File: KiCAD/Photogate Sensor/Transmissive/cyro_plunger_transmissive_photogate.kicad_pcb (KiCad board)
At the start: 2 copper layers, 122 x 70 mm, 46 parts, among them J2 FFC Socket, J3 USB_B_Micro, J4 UPDI socket, J6 Conn_01x03_Socket, Q1 Q_NMOS_GSD, Q2 Q_NMOS_GSD, Q3 Q_NMOS_GSD, Q4 Q_NMOS_GSD, U1 5V LDO, U2 Opamp_Dual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

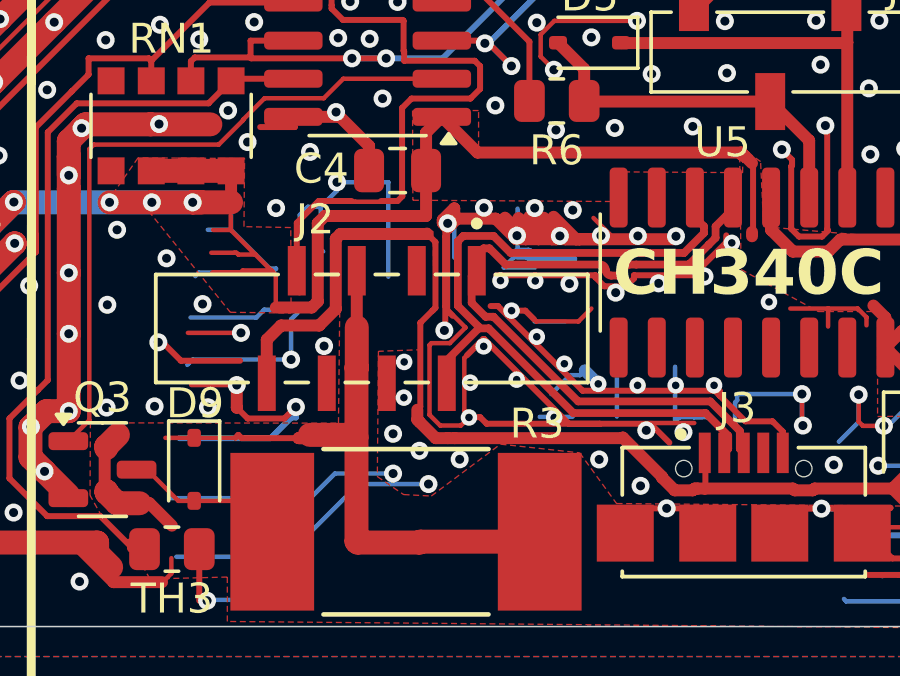
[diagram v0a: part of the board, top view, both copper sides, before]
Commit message: Place Gnds closer to data lines on FFC
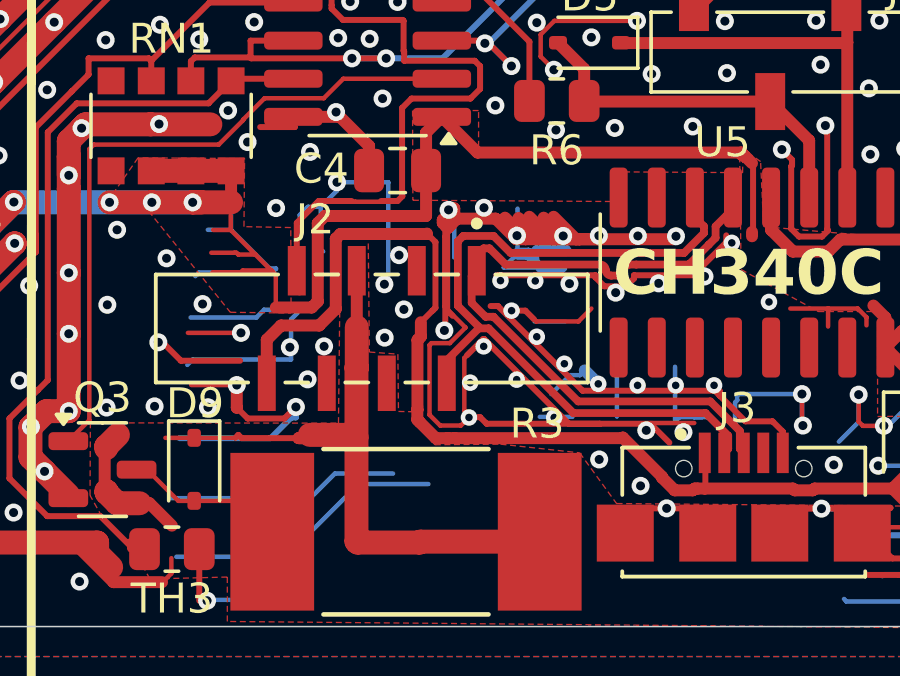
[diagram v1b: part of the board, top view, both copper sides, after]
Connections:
- J2 pad 3: +12V -> GND
- J2 pad 4: GND -> +12V
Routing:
- net GND: track 828.0 -> 827.6 mm, vias 588 -> 584

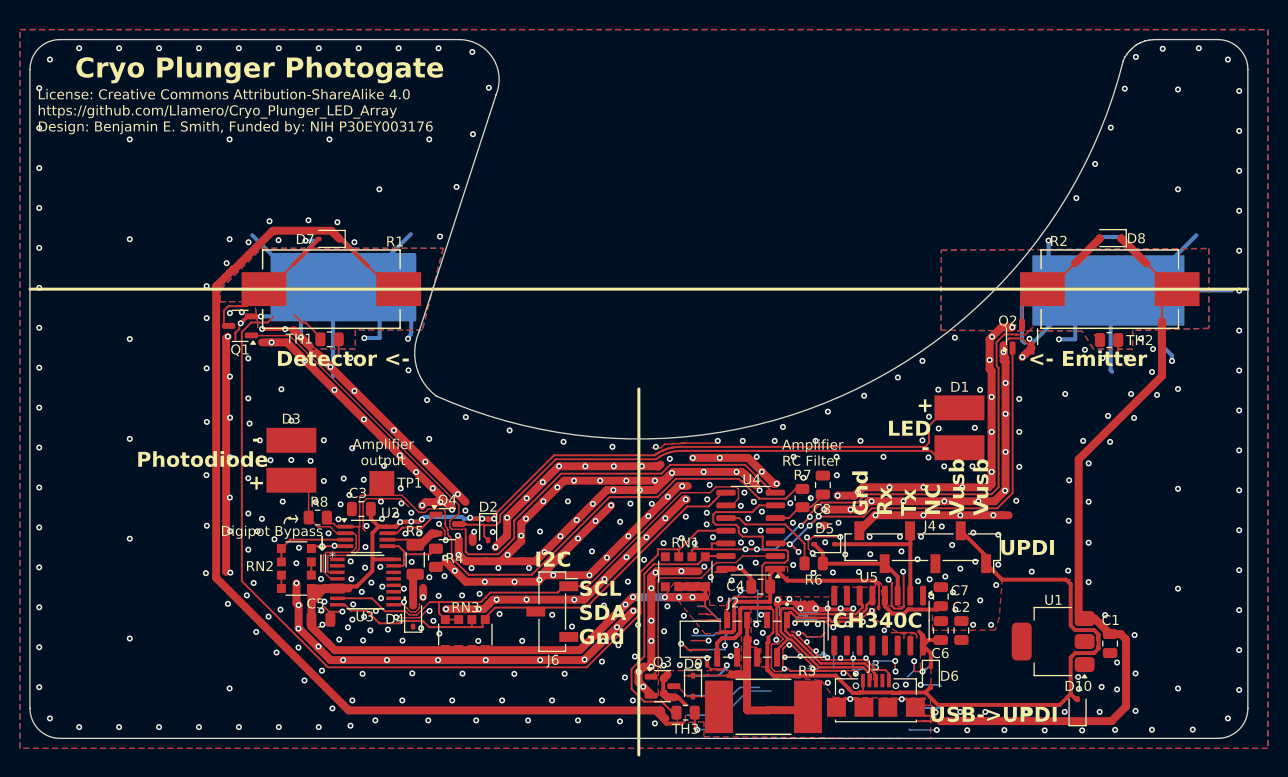
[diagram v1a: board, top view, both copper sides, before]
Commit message: More ground optimizations
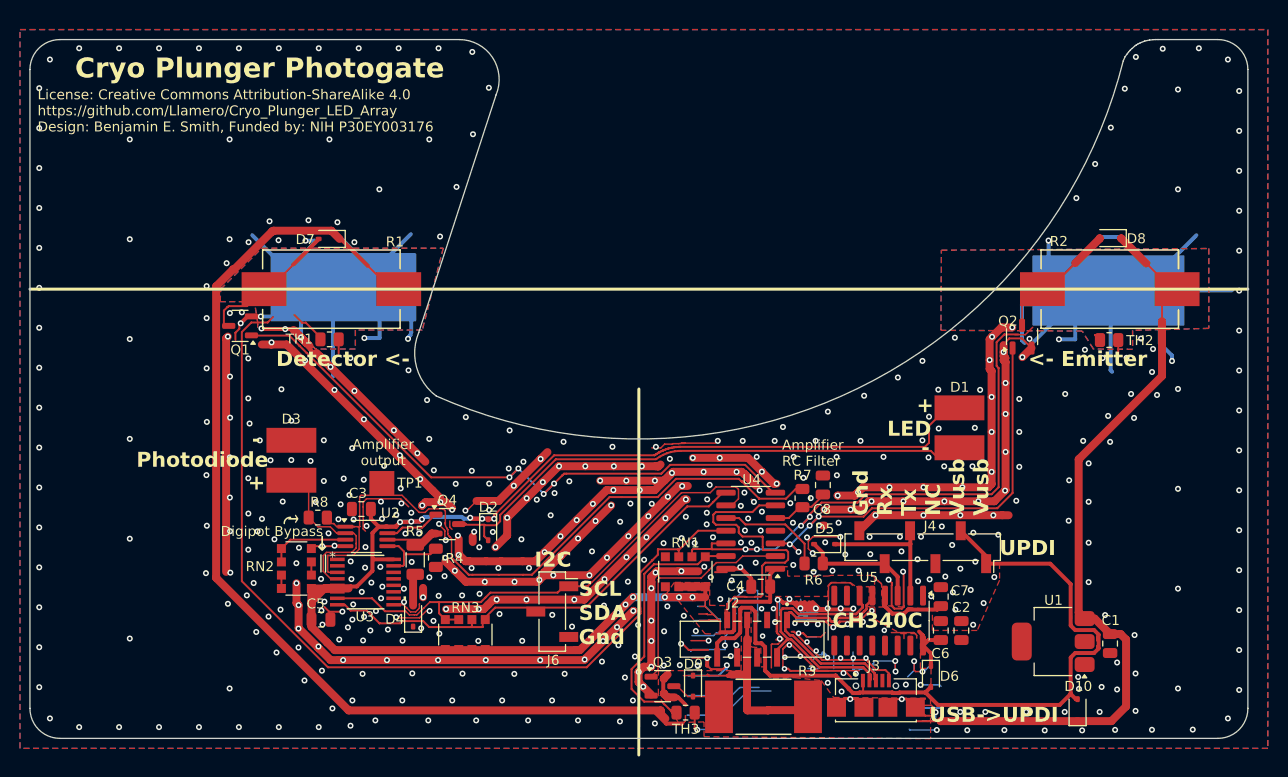
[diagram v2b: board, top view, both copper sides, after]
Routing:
- net +5V: track 185.0 -> 171.5 mm
- net GND: track 827.6 -> 816.1 mm, vias 584 -> 586
- net /Heater1: track 72.1 -> 65.8 mm, vias 0 -> 4
- net /Vusb: track 81.3 -> 80.0 mm

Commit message: Panelize boards - improve 12V thermal pad
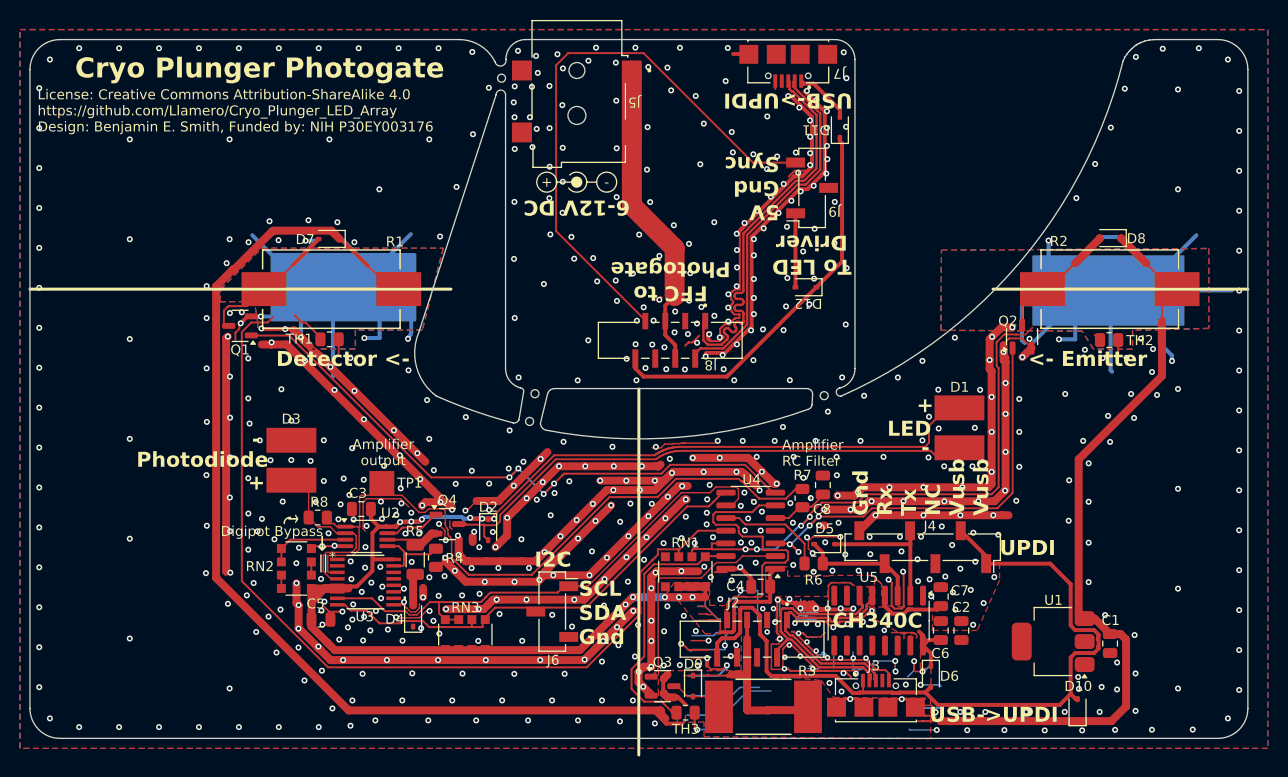
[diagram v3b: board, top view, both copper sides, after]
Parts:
- added D11: D_Schottky, Diode_SMD:D_SOD-323, F.Cu at (181.1, 108.8)
- added D12: D_Schottky, Diode_SMD:D_SOD-323, F.Cu at (177.7, 124.8)
- added H2: ~, Custom:mouse bite, F.Cu at (147.2, 103.9)
- added H3: ~, Custom:mouse bite, F.Cu at (150.6, 135.5)
- added H4: ~, Custom:mouse bite, F.Cu at (179.6, 135.7)
- added H5: ~, Custom:mouse bite, F.Cu at (150.1, 138.2)
- added J5: DC Jack, Custom:TENSILITY_54-00165, F.Cu at (154.8, 105.3)
- added J7: USB_B_Micro, Custom:CUI_UJ2-MIBH-G-SMT-TR, F.Cu at (176.0, 101.5)
- added J8: FFC Socket, Custom:AMPHENOL_SFW8S-2STE1LF, F.Cu at (164.1, 130.1)
- added J9: Conn_01x03_Socket, Connector_PinSocket_2.54mm:PinSocket_1x03_P2.54mm_Vertical_SMD_Pin1Right, F.Cu at (178.3, 114.9)
- added SYM1: Logo_Open_Hardware_Small, Custom:polarity, F.Cu at (154.6, 115.6)
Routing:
- net GND: track 816.1 -> 893.4 mm, vias 586 -> 736
- net /Comp Out: track 30.1 -> 88.5 mm
- net /D+: track 23.9 -> 64.6 mm
- net /Vusb: track 80.0 -> 118.9 mm
- net /D-: track 26.0 -> 62.1 mm
- net +12V: track 214.2 -> 245.7 mm
- net Net-(D12-A): track 0.00 -> 7.47 mm
- net Net-(D11-A): track 0.00 -> 5.77 mm
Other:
- outline, holes or cut-outs redrawn
- board text added: "5V Gnd Sync"
- board text added: "6-12V DC"
- board text added: "FFC to Photogate"
- board text added: "To LED Driver"

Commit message: replace silicon updi diode with schottky
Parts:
- D5: value D -> D_Schottky
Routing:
- net GND: vias 736 -> 739
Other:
- board text added: "Amplifier Output"
- board text removed: "Amplifier output"
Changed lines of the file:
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@@
 			)
 		)
-		(property "Value" "D"
+		(property "Value" "D_Schottky"
 			(at 0.1 1.9 0)
 			(layer "F.Fab")
@@
 			)
 		)
-		(property "Datasheet" "https://www.mccsemi.com/pdf/Products/1N4148WX(SOD-323).pdf"
+		(property "Datasheet" "https://toshiba.semicon-storage.com/info/docget.jsp?did=14077&prodName=CUS10S30"
 			(at 0 0 180)
 			(unlocked yes)
@@
 			)
 		)
-		(property "Description" "Diode 75 V 150mA Surface Mount SOD-323"
+		(property "Description" "Diode 30 V 1A Surface Mount USC"
 			(at 0 0 180)
 			(unlocked yes)
@@
 			)
 		)
-		(property "Manufacturer" "MCC (Micro Commercial Components)"
+		(property "Manufacturer" "Toshiba Semiconductor and Storage"
 			(at 0 0 180)
 			(unlocked yes)
@@
 			)
 		)
-		(property "Part" "1N4148WX-TP"
+		(property "Part" "CUS10S30,H3F"
 			(at 0 0 180)
 			(unlocked yes)
@@
 		)
 		(property "Value" "DC Jack"
-			(at 6.985 -8.8625 360)
+			(at 6.985 -8.8625 0)
 			(layer "F.Fab")
 			(effects
@@
 		)
 		(property "Footprint" "Custom:TENSILITY_54-00165"
-			(at 0 0 360)
+			(at 0 0 0)
 			(layer "F.Fab")
 			(hide yes)
@@
 		)
 		(property "Datasheet" "https://tensility.s3.us-west-2.amazonaws.com/uploads/pdffiles/54-00165.pdf"
-			(at 0 0 360)
+			(at 0 0 0)
 			(layer "F.Fab")
 			(hide yes)
@@
 		)
 		(property "Description" "Power Barrel Connector Jack 2.50mm ID (0.098\"), 5.50mm OD (0.217\") Surface Mount, Right Angle"
-			(at 0 0 360)
+			(at 0 0 0)
 			(layer "F.Fab")
 			(hide yes)
@@
 		)
 		(property "Value" "Conn_01x03_Socket"
-			(at 0 5.41 360)
+			(at 0 5.41 0)
 			(layer "F.Fab")
 			(effects
@@
 		)
 		(property "Value" "USB_B_Micro"
-			(at 9.335 -4.335 360)
+			(at 9.335 -4.335 0)
 			(layer "F.Fab")
 			(effects
@@
 		)
 		(property "Footprint" "Custom:CUI_UJ2-MIBH-G-SMT-TR"
-			(at 0 0 360)
+			(at 0 0 0)
 			(layer "F.Fab")
 			(hide yes)
@@
 		)
 		(property "Datasheet" "https://www.cuidevices.com/product/resource/uj2-mibh-g-smt-tr.pdf"
-			(at 0 0 360)
+			(at 0 0 0)
 			(layer "F.Fab")
 			(hide yes)
@@
 		)
 		(property "Description" "USB JACK, 2.0, MICRO B TYPE, 5 P"
-			(at 0 0 360)
+			(at 0 0 0)
 			(layer "F.Fab")
 			(hide yes)
@@
 		)
 		(fp_text user "PCB EDGE"
-			(at 5.325 1.325 360)
+			(at 5.325 1.325 0)
 			(layer "F.Fab")
 			(effects
@@
 		)
 		(property "Value" "D_Schottky"
-			(at 0.1 1.9 360)
+			(at 0.1 1.9 0)
 			(layer "F.Fab")
 			(effects
@@
 		)
 		(fp_text user "${REFERENCE}"
-			(at 0 -1.85 360)
+			(at 0 -1.85 0)
 			(layer "F.Fab")
 			(effects
@@
 		)
 		(fp_text user "-"
-			(at -3.2 1.35 360)
+			(at -3.2 1.35 0)
 			(layer "F.SilkS")
 			(effects
@@
 		)
 		(fp_text user "+"
-			(at 2.8 1.35 360)
+			(at 2.8 1.35 0)
 			(layer "F.SilkS")
 			(effects
@@
 		)
 		(property "Value" "FFC Socket"
-			(at 6.825 4.445 360)
+			(at 6.825 4.445 0)
 			(layer "F.Fab")
 			(effects
@@
 		)
 		(property "Footprint" "Custom:AMPHENOL_SFW8S-2STE1LF"
-			(at 0 0 360)
+			(at 0 0 0)
 			(layer "F.Fab")
 			(hide yes)
@@
 		)
 		(property "Datasheet" "https://cdn.amphenol-cs.com/media/wysiwyg/files/documentation/datasheet/flex/flexconnectors_100mm_sfw_s.pdf"
-			(at 0 0 360)
+			(at 0 0 0)
 			(layer "F.Fab")
 			(hide yes)
@@
 		)
 		(property "Description" "8 Position FFC, FPC Connector Contacts, Vertical - 1 Sided 0.039\" (1.00mm) Surface Mount"
-			(at 0 0 360)
+			(at 0 0 0)
 			(layer "F.Fab")
 			(hide yes)
@@
 	)
 	(gr_line
-		(start 161 135)
+		(start 161 138)
 		(end 160.99 171.67)
 		(stroke
@@
 		)
 	)
-	(gr_text "Amplifier\noutput"
+	(gr_text "Amplifier\nOutput"
 		(at 135.39 142.75 0)
 		(layer "F.SilkS")
@@
 	)
 	(via
+		(at 204.14 153.43)
+		(size 0.6)
+		(drill 0.3)
+		(layers "F.Cu" "B.Cu")
+		(free yes)
+		(net 2)
+	)
+	(via
 		(at 181.67 151.58)
 		(size 0.6)
@@
 	)
 	(via
+		(at 201.63 151.78)
+		(size 0.6)
+		(drill 0.3)
+		(layers "F.Cu" "B.Cu")
+		(free yes)
+		(net 2)
+	)
+	(via
 		(at 128.9 160.8)
 		(size 0.6)
@@
 		(size 0.6)
 		(drill 0.3)
+		(layers "F.Cu" "B.Cu")
+		(free yes)
+		(net 2)
+	)
+	(via
+		(at 198.01 151.78)
+		(size 0.6)
+		(drill 0.3)

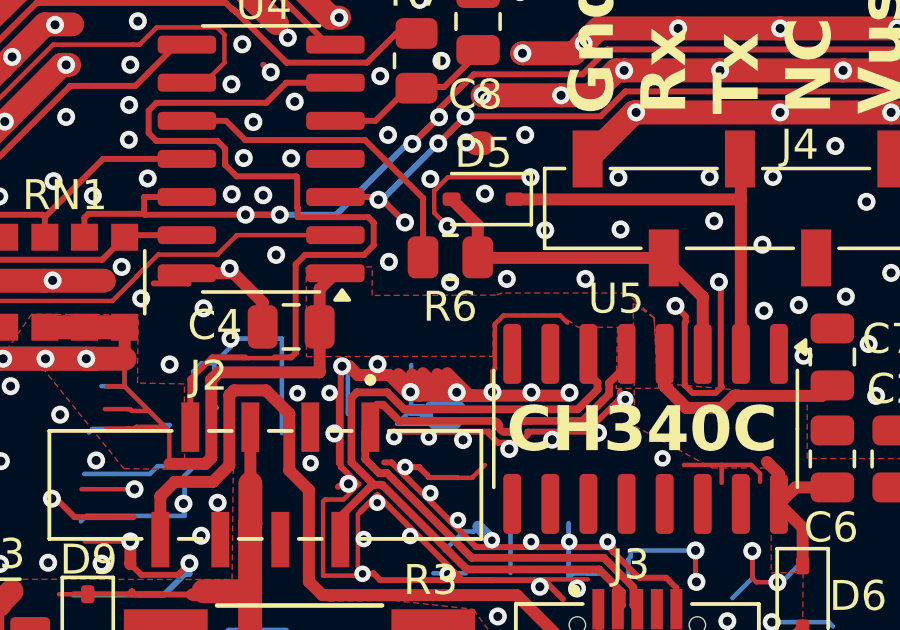
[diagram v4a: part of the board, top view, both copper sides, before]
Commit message: Add pullup to reset line
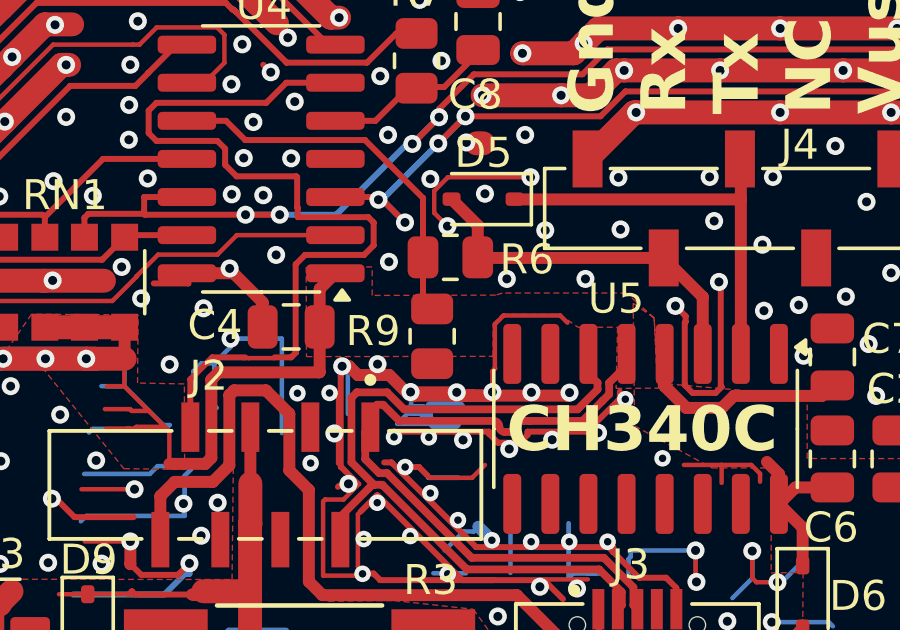
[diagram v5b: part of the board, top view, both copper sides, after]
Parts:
- added R9: 47k, Resistor_SMD:R_0805_2012Metric, F.Cu at (177.9, 155.1)
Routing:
- net GND: track 893.4 -> 888.9 mm, vias 739 -> 738
- net /UPDI: track 10.9 -> 12.8 mm

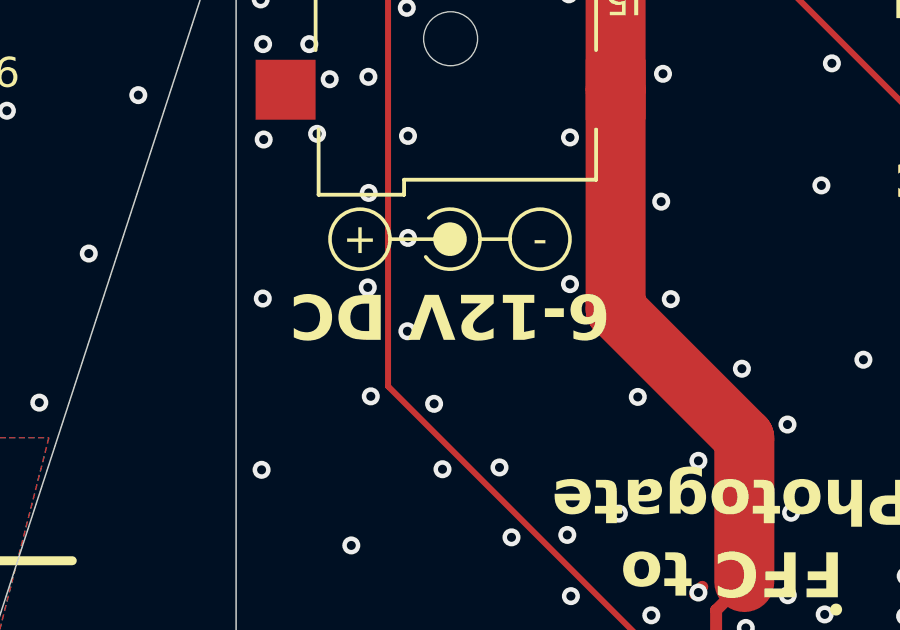
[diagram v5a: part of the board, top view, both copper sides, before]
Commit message: heater control test with autotune PWM
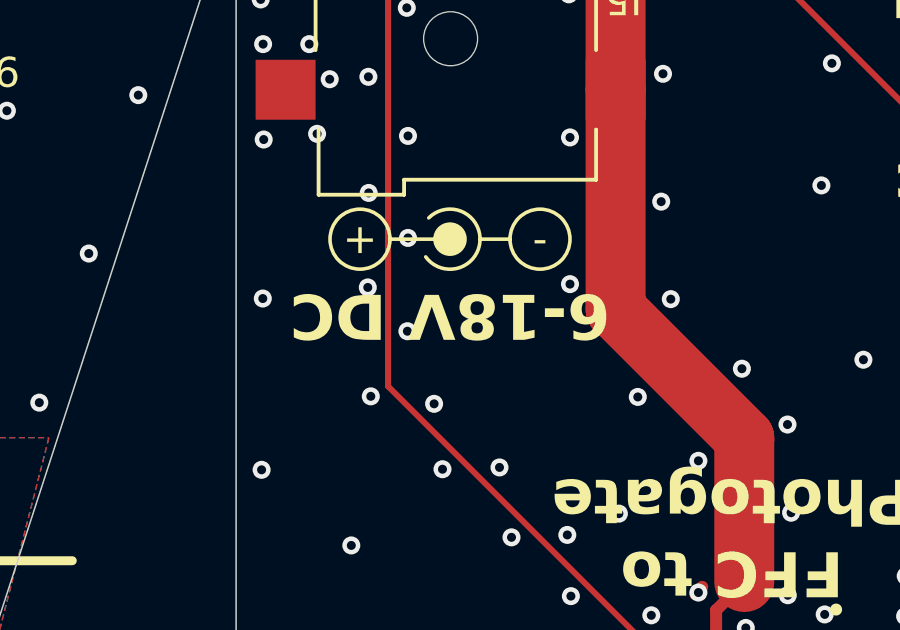
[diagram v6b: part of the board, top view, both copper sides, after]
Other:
- board text added: "6-18V DC"
- board text removed: "6-12V DC"
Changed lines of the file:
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@@
 		)
 	)
-	(gr_text "6-12V DC"
+	(gr_text "6-18V DC"
 		(at 154.77 115.953951 180)
 		(layer "F.SilkS")
